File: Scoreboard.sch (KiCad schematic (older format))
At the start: 8 parts

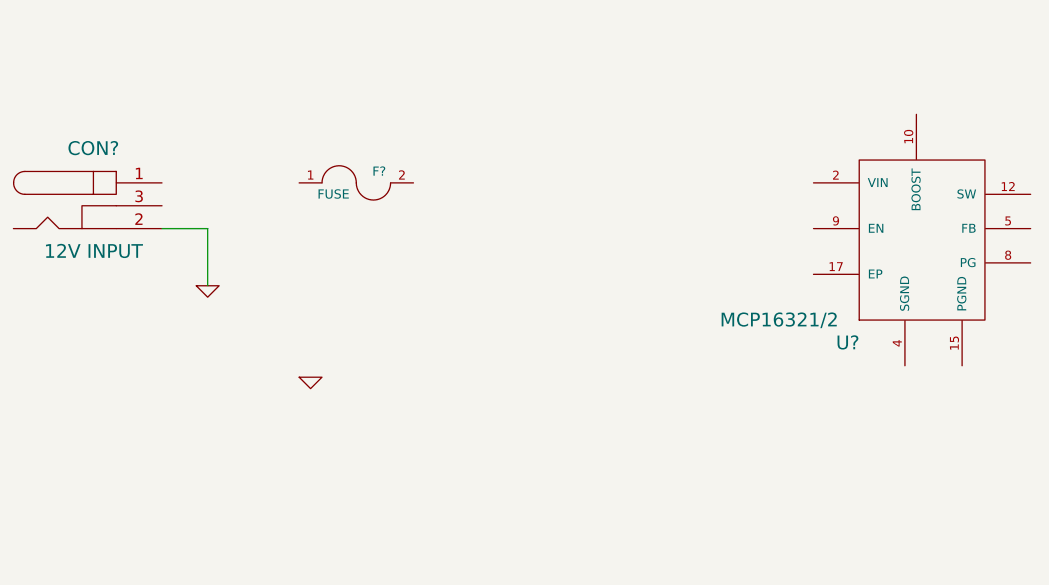
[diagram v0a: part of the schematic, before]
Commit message: Added System Diagram
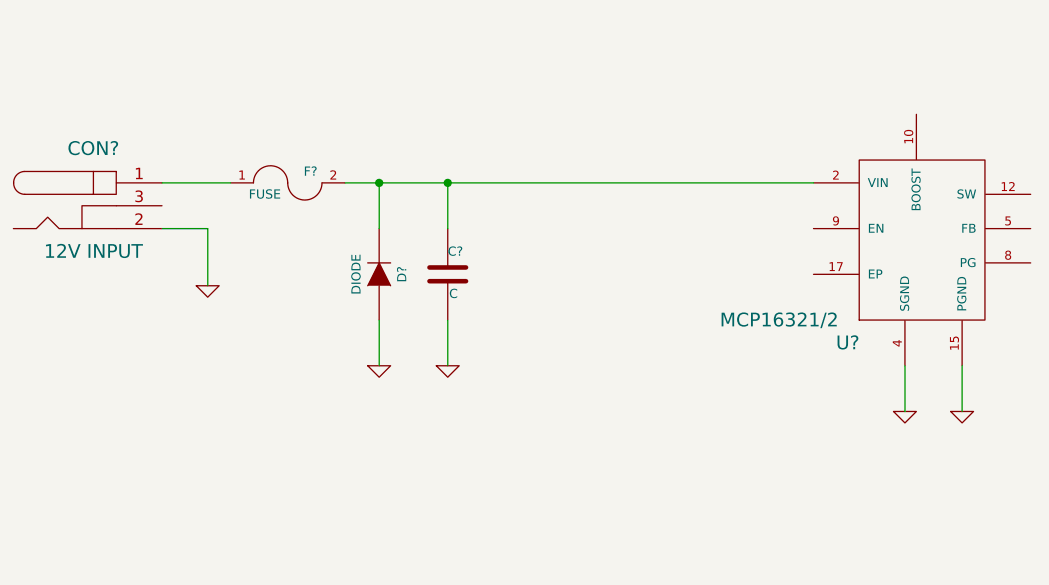
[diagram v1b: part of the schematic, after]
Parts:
- added C?: C, ~, symbol C
- added D?: DIODE, ~, symbol DIODE
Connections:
- net GND: now also U?.15 (PGND), U?.4 (SGND), C?.2, D?.1 (A)
- net at CON?.1: now also F?.1
- net at U?.2 (VIN): now also F?.2, C?.1, D?.2 (K)
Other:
- moved on the sheet: F?
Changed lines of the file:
@@
 	1    0    0    1
 $EndComp
-Wire Wire Line
-	1400 1600 1400 1450
 Text GLabel 1500 1600 1    39   BiDi ~ 0
 RD9
@@
 Text GLabel 2500 3550 3    39   Input ~ 0
 VDD_3.3V
-Wire Wire Line
-	2500 3050 2500 3550
 Text GLabel 2600 3550 3    39   Input ~ 0
 VDD_3.3V
-Wire Wire Line
-	2600 3050 2600 3550
 $Comp
 L GND #PWR?
@@
 	1    0    0    -1
 $EndComp
-Wire Wire Line
-	3300 3050 3300 3200
 $Comp
 L GND #PWR?
@@
 	1    0    0    1
 $EndComp
-Wire Wire Line
-	3300 1600 3300 1400
 $Comp
 L GND #PWR?
@@
 	1    0    0    -1
 $EndComp
-Wire Wire Line
-	1800 3050 1800 3250
 $Comp
 L GND #PWR?
@@
 	0    1    -1   0
 $EndComp
-Wire Wire Line
-	900  2100 750  2100
-Wire Wire Line
-	900  2300 750  2300
 $Comp
 L GND #PWR?
@@
 	1    0    0    -1
 $EndComp
-Wire Wire Line
-	1200 3050 1200 3250
 $Comp
 L R R1
@@
 	1    0    0    1
 $EndComp
-Wire Wire Line
-	1900 1600 1900 1350
-Wire Wire Line
-	1900 850  1900 650
 Text GLabel 3000 3250 3    39   Input ~ 0
 MCLR
-Wire Wire Line
-	3000 3250 3000 3050
 Text GLabel 3200 3250 3    39   Input ~ 0
 RB0/PGED1
 Text GLabel 3100 3250 3    39   Input ~ 0
 RB1/PGEC1
-Wire Wire Line
-	3100 3250 3100 3050
-Wire Wire Line
-	3200 3050 3200 3250
 $Comp
 L CONN_6 P?
@@
 	1    0    0    -1
 $EndComp
-Wire Wire Line
-	2800 3550 2800 3450
-Wire Wire Line
-	2800 3450 2600 3450
-Connection ~ 2600 3450
-Wire Wire Line
-	2300 3550 2300 3450
-Wire Wire Line
-	2300 3450 2500 3450
-Connection ~ 2500 3450
 Text GLabel 1850 5950 0    39   Input ~ 0
 RB0/PGED1
@@
 	0    1    -1   0
 $EndComp
-Wire Wire Line
-	2500 5650 2200 5650
-Wire Wire Line
-	1800 5750 2500 5750
-Wire Wire Line
-	2500 5850 2200 5850
-Wire Wire Line
-	1850 5950 2500 5950
-Wire Wire Line
-	2500 6050 2300 6050
 $Comp
 L BARREL_JACK CON?
@@
 	1    0    0    -1
 $EndComp
-Wire Wire Line
-	5600 1800 5800 1800
-Wire Wire Line
-	5800 1800 5800 2050
 $Comp
 L MCP16321/2 U?
@@
 L GND #PWR?
 U 1 1 53C9B69D
-P 6250 2450
-F 0 "#PWR?" H 6250 2450 30  0001 C CNN
-F 1 "GND" H 6250 2380 30  0001 C CNN
-F 2 "" H 6250 2450 60  0000 C CNN
-F 3 "" H 6250 2450 60  0000 C CNN
-	1    6250 2450
+P 6850 2400
+F 0 "#PWR?" H 6850 2400 30  0001 C CNN
+F 1 "GND" H 6850 2330 30  0001 C CNN
+F 2 "" H 6850 2400 60  0000 C CNN
+F 3 "" H 6850 2400 60  0000 C CNN
+	1    6850 2400
 	1    0    0    -1
 $EndComp
@@
 L FUSE F?
 U 1 1 53C9B6E5
-P 6450 1600
-F 0 "F?" H 6550 1650 40  0000 C CNN
-F 1 "FUSE" H 6350 1550 40  0000 C CNN
-F 2 "~" H 6450 1600 60  0000 C CNN
-F 3 "~" H 6450 1600 60  0000 C CNN
-	1    6450 1600
-	1    0    0    -1
-$EndComp
+P 6150 1600
+F 0 "F?" H 6250 1650 40  0000 C CNN
+F 1 "FUSE" H 6050 1550 40  0000 C CNN
+F 2 "~" H 6150 1600 60  0000 C CNN
+F 3 "~" H 6150 1600 60  0000 C CNN
+	1    6150 1600
+	1    0    0    -1
+$EndComp
+$Comp
+L C C?
+U 1 1 53C9B80C
+P 6850 2000
+F 0 "C?" H 6850 2100 40  0000 L CNN
+F 1 "C" H 6856 1915 40  0000 L CNN
+F 2 "~" H 6888 1850 30  0000 C CNN
+F 3 "~" H 6850 2000 60  0000 C CNN
+	1    6850 2000
+	1    0    0    -1
+$EndComp
+$Comp
+L DIODE D?
+U 1 1 53C9B825
+P 6550 2000
+F 0 "D?" H 6550 2100 40  0000 C CNN
+F 1 "DIODE" H 6550 1900 40  0000 C CNN
+F 2 "~" H 6550 2000 60  0000 C CNN
+F 3 "~" H 6550 2000 60  0000 C CNN
+	1    6550 2000
+	0    1    -1   0
+$EndComp
+$Comp
+L GND #PWR?
+U 1 1 53C9B850
+P 6550 2400
+F 0 "#PWR?" H 6550 2400 30  0001 C CNN
+F 1 "GND" H 6550 2330 30  0001 C CNN
+F 2 "" H 6550 2400 60  0000 C CNN
+F 3 "" H 6550 2400 60  0000 C CNN
+	1    6550 2400
+	1    0    0    -1
+$EndComp
+Wire Wire Line
+	1400 1600 1400 1450
+Wire Wire Line
+	2500 3050 2500 3550
+Wire Wire Line
+	2600 3050 2600 3550
+Wire Wire Line
+	3300 3050 3300 3200
+Wire Wire Line
+	3300 1600 3300 1400
+Wire Wire Line
+	1800 3050 1800 3250
+Wire Wire Line
+	900  2100 750  2100
+Wire Wire Line
+	900  2300 750  2300
+Wire Wire Line
+	1200 3050 1200 3250
+Wire Wire Line
+	1900 1600 1900 1350
+Wire Wire Line
+	1900 850  1900 650
+Wire Wire Line
+	3000 3250 3000 3050
+Wire Wire Line
+	3100 3250 3100 3050
+Wire Wire Line
+	3200 3050 3200 3250
+Wire Wire Line
+	2800 3550 2800 3450
+Wire Wire Line
+	2800 3450 2600 3450
+Connection ~ 2600 3450
+Wire Wire Line
+	2300 3550 2300 3450
+Wire Wire Line
+	2300 3450 2500 3450
+Connection ~ 2500 3450
+Wire Wire Line
+	2500 5650 2200 5650
+Wire Wire Line
+	1800 5750 2500 5750
+Wire Wire Line
+	2500 5850 2200 5850
+Wire Wire Line
+	1850 5950 2500 5950
+Wire Wire Line
+	2500 6050 2300 6050
+Wire Wire Line
+	5600 1800 5800 1800
+Wire Wire Line
+	5800 1800 5800 2050
+Wire Wire Line
+	5600 1600 5900 1600
+Wire Wire Line
+	6400 1600 8450 1600
+Wire Wire Line
+	6550 1800 6550 1600
+Connection ~ 6550 1600
+Wire Wire Line
+	6550 2400 6550 2200
+Wire Wire Line
+	6850 2200 6850 2400
+Wire Wire Line
+	6850 1800 6850 1600
+Connection ~ 6850 1600
+$Comp
+L GND #PWR?
+U 1 1 53C9B8F7
+P 8850 2600
+F 0 "#PWR?" H 8850 2600 30  0001 C CNN
+F 1 "GND" H 8850 2530 30  0001 C CNN
+F 2 "" H 8850 2600 60  0000 C CNN
+F 3 "" H 8850 2600 60  0000 C CNN
+	1    8850 2600
+	1    0    0    -1
+$EndComp
+$Comp
+L GND #PWR?
+U 1 1 53C9B906
+P 9100 2600
+F 0 "#PWR?" H 9100 2600 30  0001 C CNN
+F 1 "GND" H 9100 2530 30  0001 C CNN
+F 2 "" H 9100 2600 60  0000 C CNN
+F 3 "" H 9100 2600 60  0000 C CNN
+	1    9100 2600
+	1    0    0    -1
+$EndComp
+Wire Wire Line
+	8850 2400 8850 2600
+Wire Wire Line
+	9100 2400 9100 2600
 $EndSCHEMATC

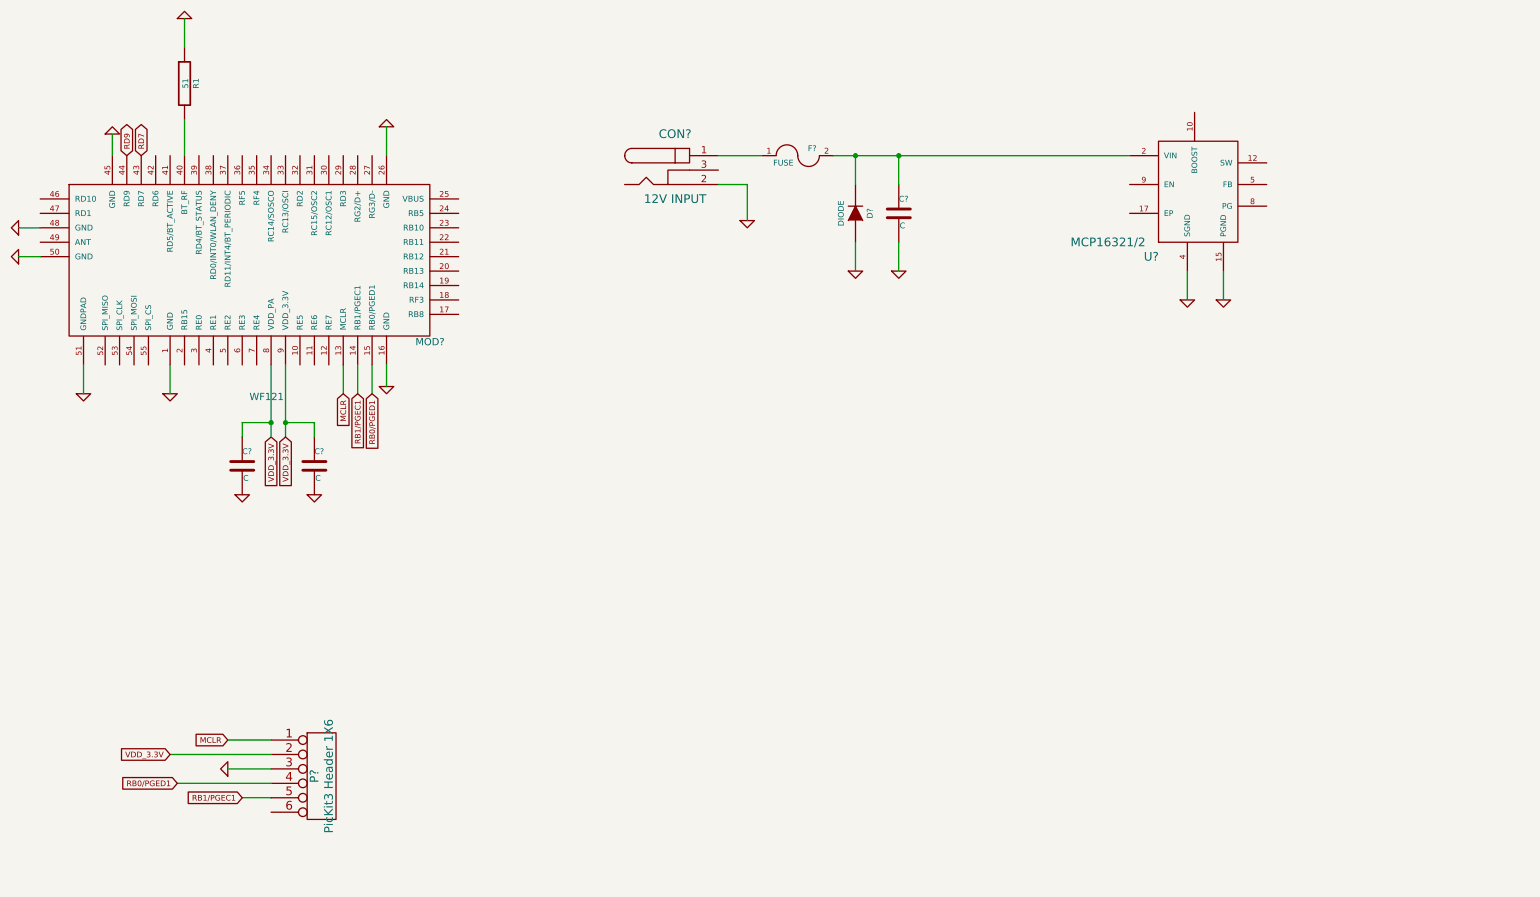
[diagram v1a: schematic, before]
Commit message: Made Sheets Started Driver Circuit
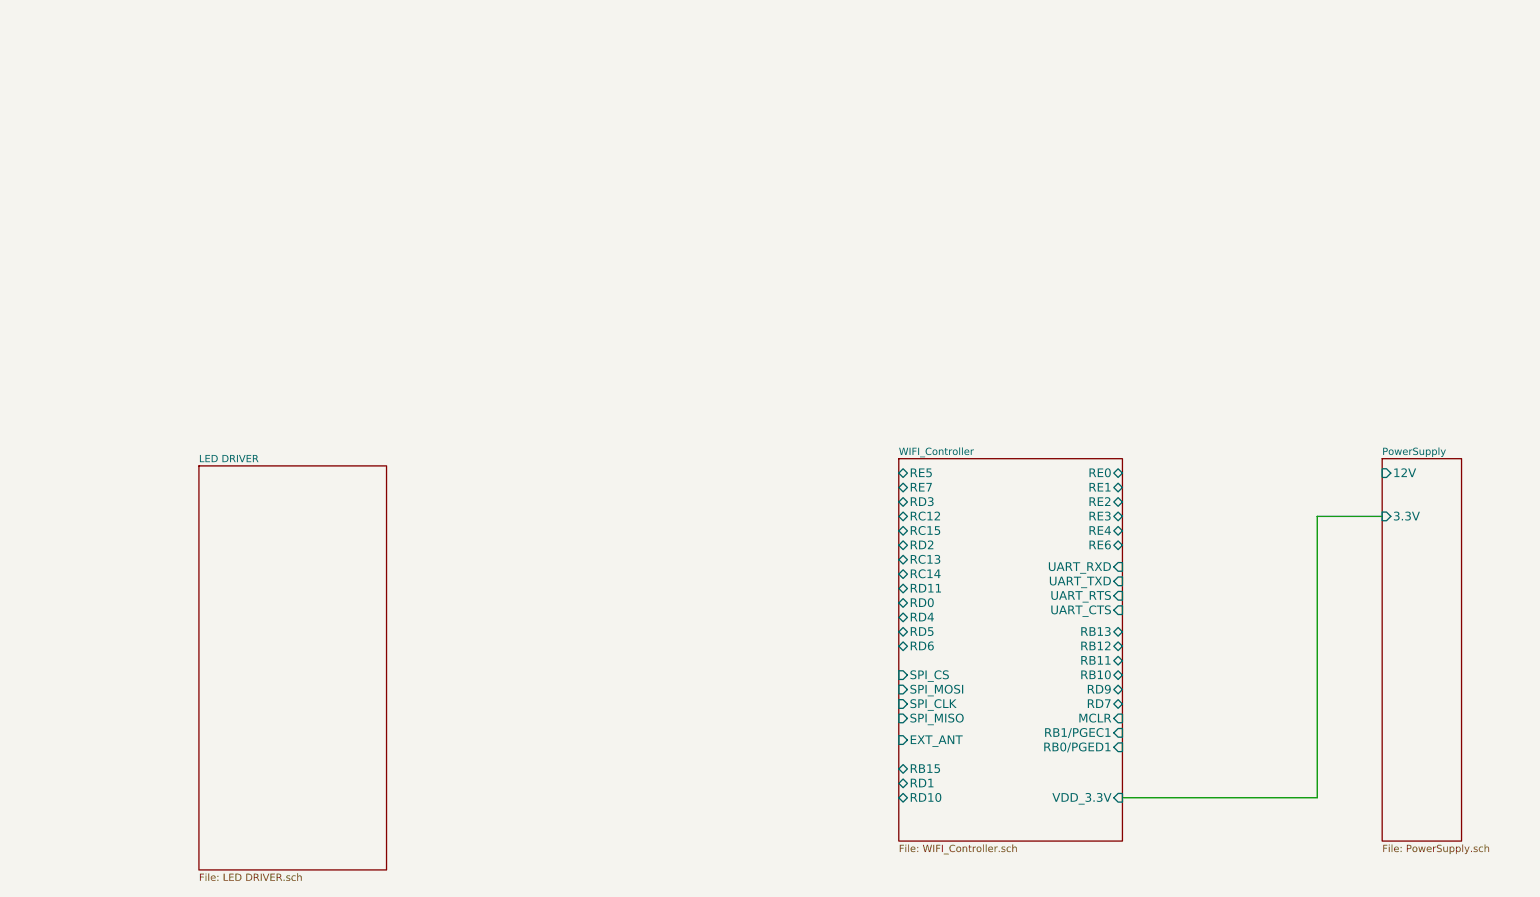
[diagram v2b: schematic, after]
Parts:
- removed C? (x3): C, ~, symbol C
- removed CON?: 12V INPUT, symbol BARREL_JACK
- removed D?: DIODE, ~, symbol DIODE
- removed F?: FUSE, ~, symbol FUSE
- removed MOD?: WF121, DIP8, symbol WF121
- removed P?: PicKit3 Header 1X6, symbol CONN_6
- removed R1: 51, ~, symbol R
- removed U?: MCP16321/2, ~, symbol MCP16321/2
